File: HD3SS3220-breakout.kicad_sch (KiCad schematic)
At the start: 15 parts, among them J1 484050003, U1 HD3SS3220IRNHR, U2 MC-312D

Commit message: Net labels
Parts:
- removed C (x6): 100nF, symbol Device:C
- removed R: 200K, symbol Device:R
- removed R (x2): 1M, symbol Device:R
- removed R: 900K, symbol Device:R
- added C (x5): 100nF, symbol Device:C_Small
- added R: 900K, symbol Device:R_Small
- C: renamed from C1; value C_Small -> 100nF
- J1: footprint Connector:Molex-0484050003 -> CONN_484050003_MOL; symbol Connector:484050003 -> Molex-0484050003:484050003
- R: renamed from R1; value R_Small -> 200K
- U1: footprint Interface_USB:HD3SS3220IRNHR -> RNH0030A; symbol Interface_USB:HD3SS3220IRNHR -> HD3SS3220IRNHR:HD3SS3220IRNHR
- U2: footprint Connector_USB:MC-312D -> footprint:USB-C-SMD_MC-312D-C; symbol Connector_USB:MC-312D -> MC-312D:MC-312D
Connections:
- net D-: now also J1.2 (D-), U2.A7 (DN1), U2.B7 (DN2)
- net GND: now also J1.4 (GND), J1.7 (GND_DRAIN), U1.12 (EN_MUX_N), U1.13 (GND), U1.28 (GND), U1.29 (EN_CC_N), U1.3 (CURRENT_MODE), U1.31 (PAD), U2.1 (SHIELD), U2.2 (SHIELD), U2.3 (SHIELD), U2.4 (SHIELD), U2.A1 (GND), U2.A12 (GND), U2.B1 (GND), U2.B12 (GND)
- net VBUS: now also J1.1 (VBUS), U1.30 (VDD5), U2.A4 (VBUS), U2.A9 (VBUS), U2.B4 (VBUS), U2.B9 (VBUS), R.1
- net VCC 3.3V: now also R.1, U1.8 (VCC33)
- net TX2-: now reaches C.1
- net TX2-: now also U2.B3 (SSTXN2)
- net at C.2: now also U1.20 (TX2N)
- net at R.2: now also U1.11 (DIR)
- new net: C.2, U1.17 (TX1P)
- new net: U1.1 (CC2), U2.B5 (CC2)
- new net: C.2, U1.16 (TX1N)
- new net: U1.2 (CC1), U2.A5 (CC1)
- new net: C.2, U1.21 (TX2P)
- new net: R.2, U1.5 (VBUS_DET)
- new net: C.1, U1.6 (TXP)
- new net: C.1, U1.7 (TXN)
- new net D+: J1.3 (D+), U2.A6 (DP1), U2.B6 (DP2)
- new net RX1+: U1.15 (RX1P), U2.B11 (SSRXP1)
- new net RX1-: U1.14 (RX1N), U2.B10 (SSRXN1)
- new net RX2+: U1.19 (RX2P), U2.A11 (SSRXP2)
- new net RX2-: U1.18 (RX2N), U2.A10 (SSRXN2)
- new net SSRX+: J1.6 (SSRX+), U1.9 (RXP)
- new net SSRX-: J1.5 (SSRX-), U1.10 (RXN)
- new net SSTX+: C.2, J1.9 (SSTX+)
- new net SSTX-: C.2, J1.8 (SSTX-)
- new net TX1+: C.1, U2.A2 (SSTXP1)
- new net TX1-: C.1, U2.A3 (SSTXN1)
- new net TX2+: C.1, U2.B2 (SSTXP2)
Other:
- note removed: "check if it needs capacitor"
- note removed: "remove"
- note removed: "reorganize: shield ground etc"
- note removed: "use small ones"
- note removed: "vbus is 5v"
- note removed: "wires spanning whole page"
- moved on the sheet: C, R

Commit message: further reorganizaing
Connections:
- net GND: no longer U1.3 (CURRENT_MODE)
- net CC1: now reaches U1.1 (CC2)
- net CC1: now also U2.A5 (CC1); no longer U2.B5 (CC2)
- net CC2: now reaches U1.2 (CC1)
- net CC2: now also U2.B5 (CC2); no longer U2.A5 (CC1)
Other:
- note added: "add low dropout regulator - 5v to 3v"
- note added: "power flags"
- note added: "refactor - kicad default symbol"
- note added: "rule area for marking impedence match pairs"
- moved on the sheet: C, J1, R, U1, U2

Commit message: switches and ldo
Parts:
- removed U2: MC-312D, footprint:USB-C-SMD_MC-312D-C, symbol MC-312D:MC-312D
- added C: 3.3uF, symbol Device:C_Small
- added C: 10nF, symbol Device:C_Small
- added C: 1uF, symbol Device:C_Small
- added J2: USB_C_Receptacle, symbol Connector:USB_C_Receptacle
- added R1: 10K, symbol Device:R_Small
- added R2: 500K, symbol Device:R_Small
- added R3: 1K, symbol Device:R_Small
- added SW1: SW_DIP_x04, symbol Switch:SW_DIP_x04
- added U2: LT1962-3.3, Package_SO:MSOP-8_3x3mm_P0.65mm, symbol Regulator_Linear:LT1962-3.3
- added U3: PZ254-2-08-WS, footprint:HDR-SMD_16P-P2.54-H-M-R2-C8-W12.0-N, symbol PZ254-2-08-WS:PZ254-2-08-WS
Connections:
- net CC1: now also J2.A5 (CC1)
- net CC2: now also J2.B5 (CC2)
- net D+: now also J2.A6 (D+), J2.B6 (D+)
- net D-: now also J2.A7 (D-), J2.B7 (D-)
- net GND: now also C.2, J2.A1 (GND), J2.A12 (GND), J2.B1 (GND), J2.B12 (GND), J2.S1 (SHIELD), SW1.1, U2.4 (GND)
- net RX1+: now also J2.B11 (RX1+)
- net RX1-: now also J2.B10 (RX1-)
- net RX2+: now also J2.A11 (RX2+)
- net RX2-: now also J2.A10 (RX2-)
- net SSTX+: now also U1.3 (CURRENT_MODE), R1.2, R2.2
- net TX1+: now also J2.A2 (TX1+)
- net TX1-: now also J2.A3 (TX1-)
- net TX2+: now also J2.B2 (TX2+)
- net TX2-: now also J2.B3 (TX2-)
- net VBUS: now also C.2, J2.A4 (VBUS), J2.A9 (VBUS), J2.B4 (VBUS), J2.B9 (VBUS), R3.1, SW1.3, SW1.4, U2.5 (~{SHDN})
- net at U1.22 (ADDR): now also U3.10
- net at U1.23 (INT_OUT3_N): now also U3.6
- net at U1.24 (VCONN_FAULT_N): now also U3.12
- net at U1.25 (SDA_OUT1): now also U3.14
- net at U1.26 (SCL_OUT2): now also U3.16
- net at U1.27 (ID): now also U3.8
- net at U1.4 (PORT): now also SW1.7, SW1.8
- net VCC 3.3V: no longer names the net of R.1, U1.8 (VCC33)
- net VCC 3.3V: now also C.1, U2.2 (SENSE)
- new net: R1.1, SW1.5
- new net: R3.2, SW1.2
- new net: R2.1, SW1.6
- new net: C.2, U2.1 (OUT)
- new net: C.1, U2.3 (BYP)
- new net: C.1, U2.8 (IN)
- no-connect marks 9 -> 2
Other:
- note removed: "add low dropout regulator - 5v to 3v"
- note removed: "dip switch"
- note removed: "put to pin header"
- note removed: "refactor - kicad default symbol"
- moved on the sheet: C, J1, R, U1

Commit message: post review on 02/27/2026
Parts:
- added U4: HD3SS3220RNHR, footprint:WQFN-30_L4.5-W2.5-P0.4-BL-EP, symbol Interface_USB:HD3SS3220RNHR
- added U5: U-A-39SS-Y-1, footprint:USB-3.0-A_U-A-39SS-Y-1, symbol Connector_USB-custom:U-A-39SS-Y-1
- added U6: HT7533-1_C14289, footprint:SOT-89-3_L4.5-W2.5-P1.50-LS4.2-BR, symbol Regulator_Linear:HT7533-1_C14289
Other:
- note added: "Configuration DIP switches"
- note added: "ESD diodes goes in here"
- note added: "LDO 5v => 3v3"
- note added: "USB 2:1 SuperSpeed Mux"
- note added: "USB-A 3.0 Connector"
- note added: "USB-C 3.0 Connector"
- note added: "label names for different pins"
- note added: "pin header 2x8"
- moved on the sheet: C, J1, J2, R, R1, R2, R3, SW1, U1, U2, U3

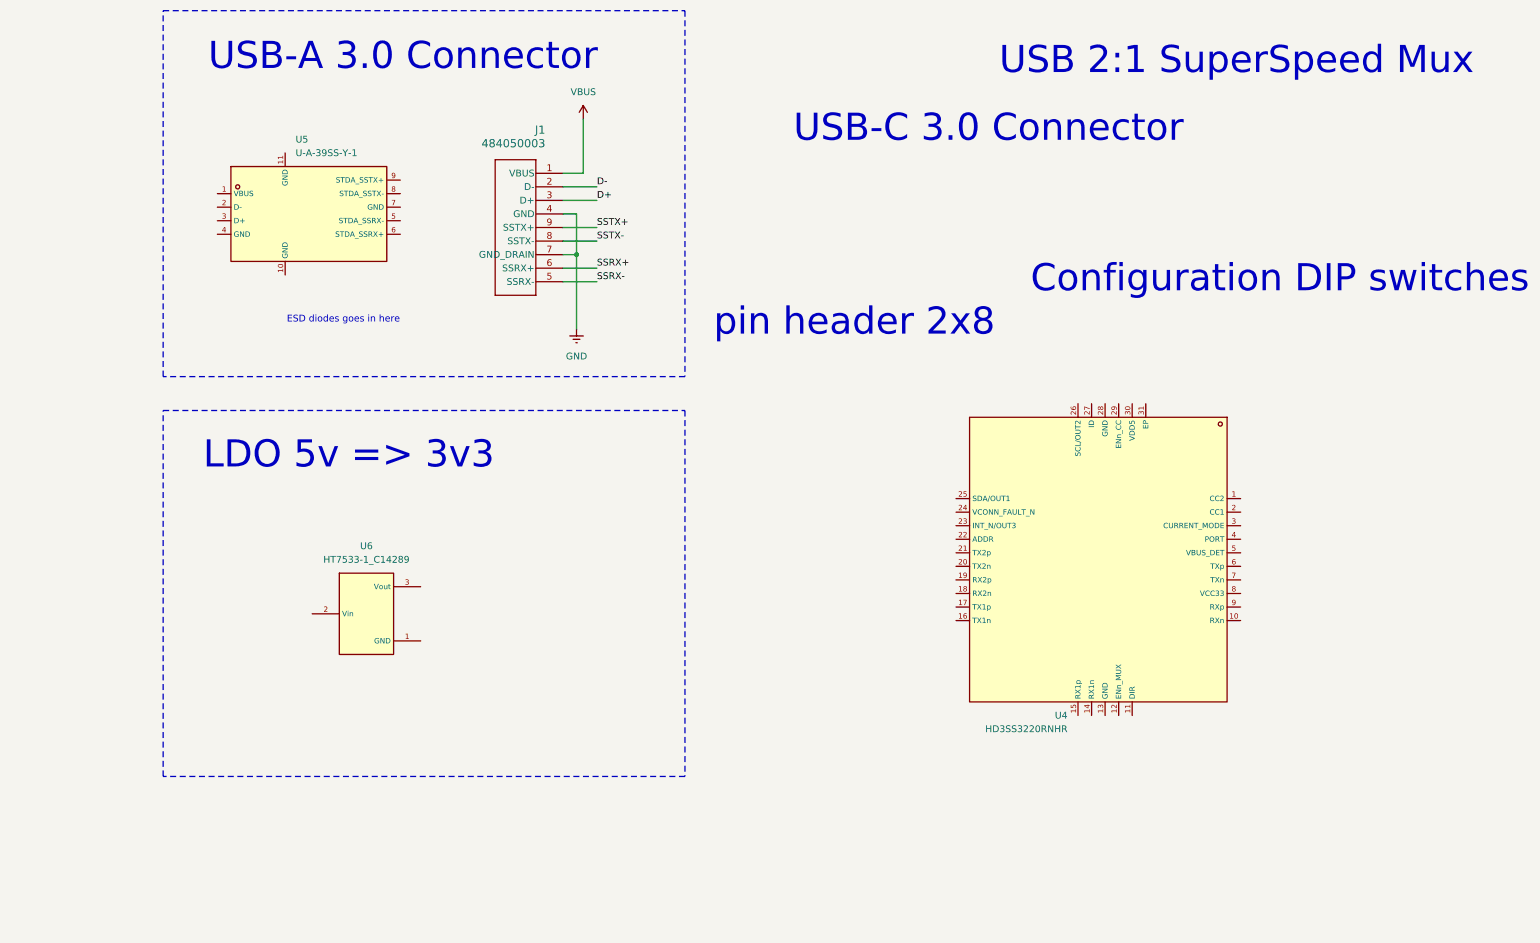
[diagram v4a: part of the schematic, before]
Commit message: usb-a 3.0 connector
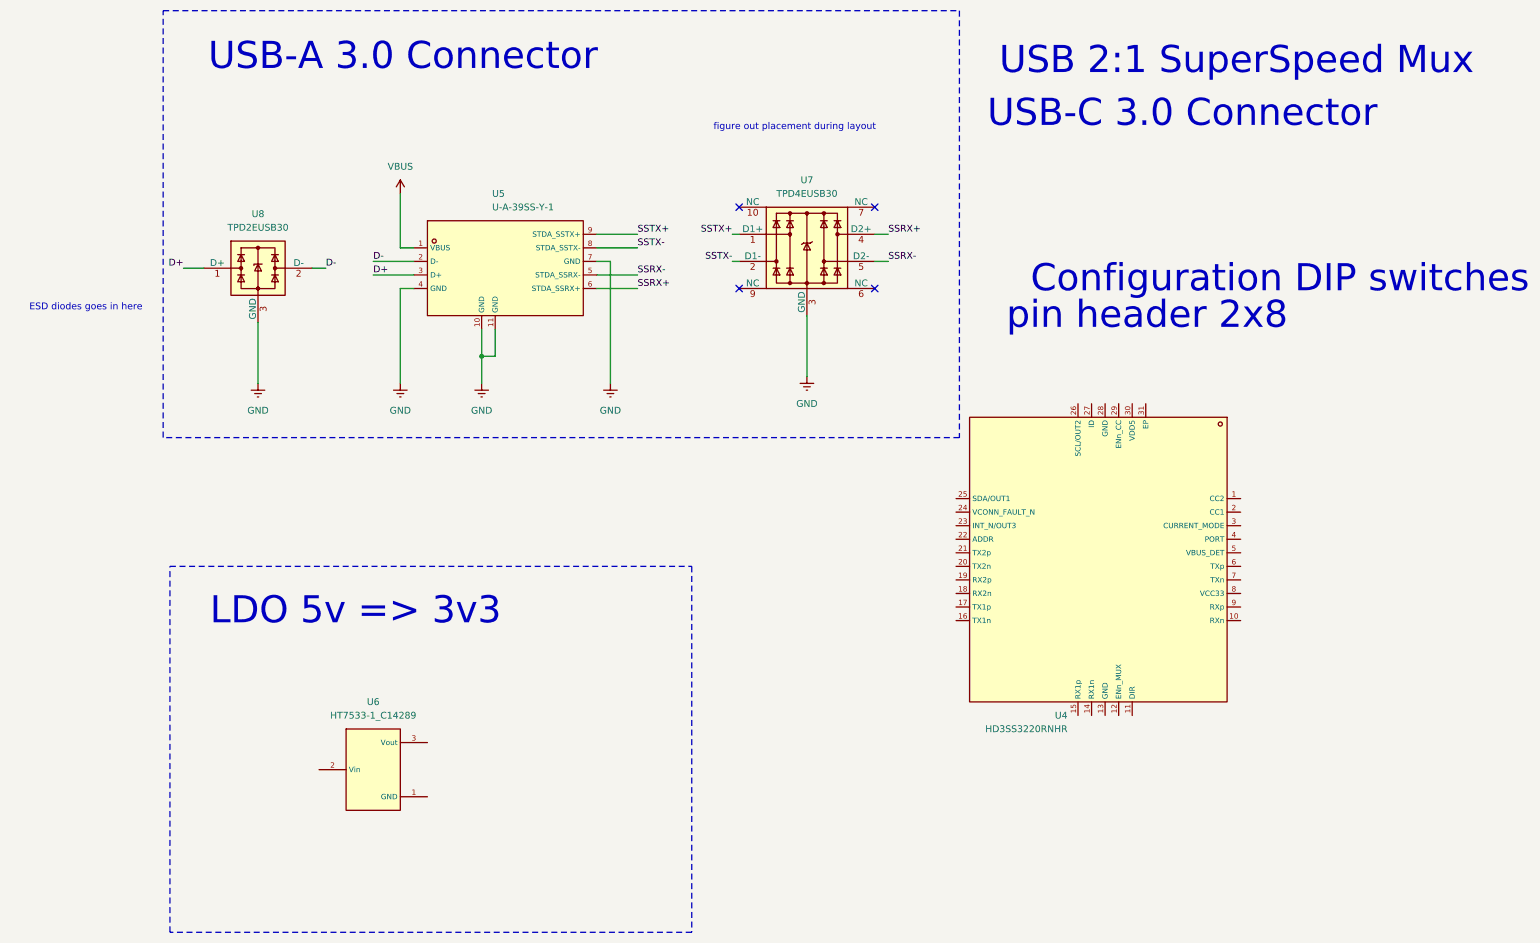
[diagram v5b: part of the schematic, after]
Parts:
- removed J1: 484050003, CONN_484050003_MOL, symbol Molex-0484050003:484050003
- added U7: TPD4EUSB30, Package_SON:USON-10_2.5x1.0mm_P0.5mm, symbol Power_Protection:TPD4EUSB30
- added U8: TPD2EUSB30, Package_TO_SOT_SMD:Texas_DRT-3, symbol Power_Protection:TPD2EUSB30
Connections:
- net D+: now also U5.3 (D+), U8.1 (D+)
- net D-: now also U5.2 (D-), U8.2 (D-)
- net GND: now also U5.10 (GND), U5.11 (GND), U5.4 (GND), U5.7 (GND), U7.3 (GND), U7.8 (GND), U8.3 (GND)
- net SSRX+: now also U5.6 (STDA_SSRX+), U7.4 (D2+)
- net SSRX-: now also U5.5 (STDA_SSRX-), U7.5 (D2-)
- net SSTX+: now also U5.9 (STDA_SSTX+), U7.1 (D1+)
- net SSTX-: now also U5.8 (STDA_SSTX-), U7.2 (D1-)
- net VBUS: now also U5.1 (VBUS)
- no-connect marks 2 -> 6
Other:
- note added: "figure out placement during layout"
- moved on the sheet: U5, U6

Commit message: all reorged
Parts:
- removed C (x6): 100nF, symbol Device:C_Small
- removed C: 3.3uF, symbol Device:C_Small
- removed C: 10nF, symbol Device:C_Small
- removed C: 1uF, symbol Device:C_Small
- removed R: 200K, symbol Device:R_Small
- removed R: 900K, symbol Device:R_Small
- removed R1: 10K, symbol Device:R_Small
- removed R2: 500K, symbol Device:R_Small
- removed R3: 1K, symbol Device:R_Small
- removed SW1: SW_DIP_x04, symbol Switch:SW_DIP_x04
- removed U1: HD3SS3220IRNHR, RNH0030A, symbol HD3SS3220IRNHR:HD3SS3220IRNHR
- removed U2: LT1962-3.3, Package_SO:MSOP-8_3x3mm_P0.65mm, symbol Regulator_Linear:LT1962-3.3
- removed U3: PZ254-2-08-WS, footprint:HDR-SMD_16P-P2.54-H-M-R2-C8-W12.0-N, symbol PZ254-2-08-WS:PZ254-2-08-WS
- added C1, C3, C4, C5: 100nF, symbol Device:C_Small
- added C11, C12: 10uF, symbol Device:C_Small
- added R10: 200K, symbol Device:R_Small
- added R6: 1K, symbol Device:R_Small
- added R7: 500K, symbol Device:R_Small
- added R8: 10K, symbol Device:R_Small
- added R9: 900K, symbol Device:R_Small
- added SW2: SW_DIP_x04, symbol Switch:SW_DIP_x04
- added U9: PZ254-2-08-WS, footprint:HDR-SMD_16P-P2.54-H-M-R2-C8-W12.0-N, symbol PZ254-2-08-WS:PZ254-2-08-WS
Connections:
- net CC1: now also U4.2 (CC1)
- net CC2: now also U4.1 (CC2)
- net GND: now also U4.12 (ENn_MUX), U4.13 (GND), U4.28 (GND), U4.29 (ENn_CC), U4.31 (EP), U6.1 (GND), SW2.1
- net RX1+: now also U4.15 (RX1p)
- net RX1-: now also U4.14 (RX1n)
- net RX2+: now also U4.19 (RX2p)
- net RX2-: now also U4.18 (RX2n)
- net SSRX+: now also U4.9 (RXp)
- net SSRX-: now also U4.10 (RXn)
- net SSTX+: now also C4.2
- net SSTX-: now also C5.2
- net TX1+: now also U4.17 (TX1p)
- net TX1-: now also U4.16 (TX1n)
- net TX2+: now also C1.1
- net TX2-: now also C3.1
- net VBUS: now also U4.30 (VDD5), C12.2, R6.1, R9.1, SW2.3, SW2.4
- net at U4.11 (DIR): now also R10.2
- net at U4.20 (TX2n): now also C3.2
- net at U4.21 (TX2p): now also C1.2
- net ADDR: now reaches U4.22 (ADDR)
- net ADDR: now also U9.10
- net INT_N: now reaches U4.23 (INT_N/OUT3)
- net INT_N: now also U9.6
- net VCONN: now reaches U4.24 (VCONN_FAULT_N)
- net VCONN: now also U9.12
- net SDA: now reaches U4.25 (SDA/OUT1)
- net SDA: now also U9.14
- net SCL: now reaches U4.26 (SCL/OUT2)
- net SCL: now also U9.16
- net ID: now reaches U4.27 (ID)
- net ID: now also U9.8
- net MODE: now reaches U4.3 (CURRENT_MODE)
- net MODE: now also R7.2, R8.2
- net PORT: now reaches U4.4 (PORT)
- net PORT: now also SW2.7, SW2.8
- net at U4.5 (VBUS_DET): now also R9.2
- net at U4.6 (TXp): now also C4.1
- net at U4.7 (TXn): now also C5.1
- net V_out: now reaches U4.8 (VCC33)
- net V_out: now also C11.1, R10.1
- net at U6.2 (Vin): now also C12.1
- net at U6.3 (Vout): now also C11.2
- new net: R6.2, SW2.2
- new net: R7.1, SW2.6
- new net: R8.1, SW2.5
- no-connect marks 6 -> 16
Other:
- note removed: "ESD diodes goes in here"
- note removed: "label names for different pins"
- moved on the sheet: J2, U4, U5, U6, U7, U8

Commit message: notes
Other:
- note added: "1 nor 2 closed: NC - DRP 1 closed: Low - UFP 2 closed: High - DFP 3 nor 4 closed: Default - 900mA 3 closed: Medium - 1.5A 4 closed: High - 3A"
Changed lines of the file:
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@@
+		)
+	)
+	(text "1 nor 2 closed: NC - DRP\n1 closed: Low - UFP\n2 closed: High - DFP\n3 nor 4 closed: Default - 900mA\n3 closed: Medium - 1.5A\n4 closed: High - 3A"
+		(exclude_from_sim no)
+		(at 257.302 145.542 0)
+		(effects
+			(font
+				(size 1.27 1.27)
+			)
 		)
 	)
